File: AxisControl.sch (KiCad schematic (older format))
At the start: 2 parts, among them J14 Max, J15 Min

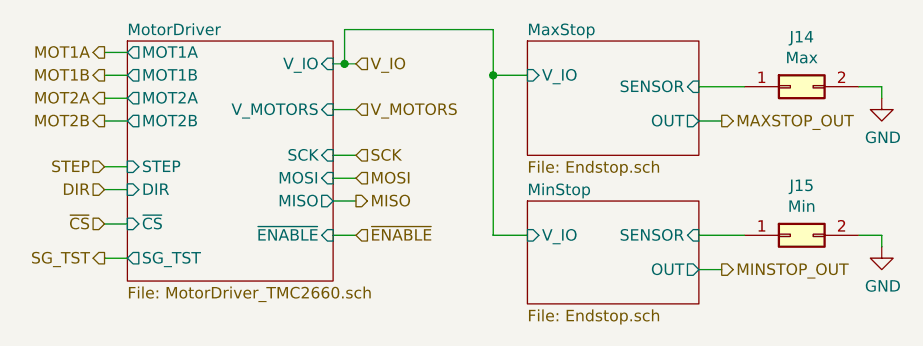
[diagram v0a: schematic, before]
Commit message: Added clock line for the motor drivers.
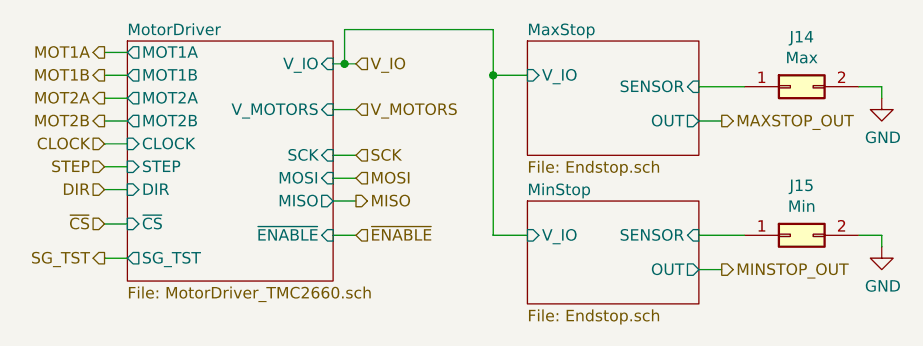
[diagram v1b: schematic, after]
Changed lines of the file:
@@
 F14 "~ENABLE" I R 4450 4000 50
 F15 "SG_TST" O L 3550 4100 50
+F16 "CLOCK" I L 3550 3600 50
 $EndSheet
 Text HLabel 3450 3200 0    50   Output ~ 0
@@
 AR Path="/5AC337B6/5ACCA309/5AE0BC50" Ref="#PWR034"  Part="1"
 AR Path="/5AC337B6/5ACE1C6D/5AE0BC50" Ref="#PWR045"  Part="1"
-F 0 "#PWR045" H 6850 3150 50  0001 C CNN
+F 0 "#PWR023" H 6850 3150 50  0001 C CNN
 F 1 "GND" H 6855 3227 50  0000 C CNN
 F 2 "" H 6850 3400 50  0001 C CNN
@@
 AR Path="/5AC337B6/5ACCA309/5AE0BC78" Ref="#PWR035"  Part="1"
 AR Path="/5AC337B6/5ACE1C6D/5AE0BC78" Ref="#PWR046"  Part="1"
-F 0 "#PWR046" H 6850 3800 50  0001 C CNN
+F 0 "#PWR024" H 6850 3800 50  0001 C CNN
 F 1 "GND" H 6855 3877 50  0000 C CNN
 F 2 "" H 6850 4050 50  0001 C CNN
@@
 Wire Wire Line
 	6250 3350 6050 3350
+Text HLabel 3450 3600 0    50   Input ~ 0
+CLOCK
+Wire Wire Line
+	3450 3600 3550 3600
 $EndSCHEMATC
